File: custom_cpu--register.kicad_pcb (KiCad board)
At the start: 2 copper layers, 100 x 63 mm, 45 parts, among them P1 CONN_01X01, P10 CONN_01X01, P11 CONN_01X01, P12 CONN_01X01, P13 CONN_01X01, P14 CONN_01X01, P15 CONN_01X01, P16 CONN_01X01, P17 CONN_01X01, P18 CONN_01X01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

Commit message: Finish preliminary design
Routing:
- net VCC: track 0.00 -> 118.2 mm, vias 0 -> 3
- net Net-(P7-Pad1): track 0.00 -> 75.4 mm, vias 0 -> 3
- net Net-(P5-Pad1): track 0.00 -> 64.7 mm
- net Net-(P12-Pad1): track 0.00 -> 60.7 mm, vias 0 -> 1
- net Net-(D8-Pad2): track 0.00 -> 59.7 mm, vias 0 -> 1
- net Net-(P1-Pad1): track 0.00 -> 57.0 mm, vias 0 -> 2
- net Net-(D1-Pad2): track 0.00 -> 52.3 mm, vias 0 -> 2
- net Net-(P6-Pad1): track 0.00 -> 52.0 mm, vias 0 -> 2
- net Net-(D7-Pad2): track 0.00 -> 51.6 mm, vias 0 -> 2
- net Net-(P8-Pad1): track 0.00 -> 49.8 mm, vias 0 -> 2
- net Net-(P2-Pad1): track 0.00 -> 49.1 mm, vias 0 -> 2
- net Net-(P13-Pad1): track 0.00 -> 45.5 mm
- net Net-(D6-Pad2): track 0.00 -> 44.2 mm, vias 0 -> 2
- net Net-(P9-Pad1): track 0.00 -> 43.9 mm, vias 0 -> 2
- net Net-(D2-Pad2): track 0.00 -> 42.5 mm, vias 0 -> 2
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- added copper zone on B.Cu, net GND
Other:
- board text added: "CPU Register"
- board text added: "Fake resistors, use wire"
- board text added: "Register design - Ben Eater KiCAD layout - Leland Batey"

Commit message: Tweak trace layout, add PNG version of layout
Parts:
- moved P23 0.27 mm to (54.0, 55.3)
- moved P25 0.27 mm to (146.0, 55.3)
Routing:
- net Net-(D8-Pad2): track 59.7 -> 56.0 mm
- net VCC: track 118.2 -> 121.5 mm
- net Net-(D1-Pad2): track 52.3 -> 54.4 mm
- net Net-(D3-Pad2): track 35.2 -> 37.0 mm
- net Net-(D6-Pad2): track 44.2 -> 46.0 mm
- net Net-(D2-Pad2): track 42.5 -> 44.3 mm
- net Net-(D4-Pad2): track 30.7 -> 32.1 mm
- net Net-(D5-Pad2): track 40.0 -> 40.9 mm

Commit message: Make labels consistent with original design, add README
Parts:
- removed P1, P14, P15, P16, P17, P18, P19, P2, P20, P21, P3, P4, P5, P6, P7, P8: CONN_01X01, Connectors:PINTST
- added D_inpt_1: CONN_01X01, Connectors:PINTST, F.Cu at (54.0, 65.0)
- added D_inpt_2: CONN_01X01, Connectors:PINTST, F.Cu at (54.0, 69.0)
- added D_inpt_3: CONN_01X01, Connectors:PINTST, F.Cu at (54.0, 73.0)
- added D_inpt_4: CONN_01X01, Connectors:PINTST, F.Cu at (54.0, 77.0)
- added D_inpt_5: CONN_01X01, Connectors:PINTST, F.Cu at (54.0, 85.0)
- added D_inpt_6: CONN_01X01, Connectors:PINTST, F.Cu at (54.0, 89.0)
- added D_inpt_7: CONN_01X01, Connectors:PINTST, F.Cu at (54.0, 93.0)
- added D_inpt_8: CONN_01X01, Connectors:PINTST, F.Cu at (54.0, 97.0)
- added D_outpt_1: CONN_01X01, Connectors:PINTST, F.Cu at (147.0, 67.0)
- added D_outpt_2: CONN_01X01, Connectors:PINTST, F.Cu at (147.0, 71.0)
- added D_outpt_3: CONN_01X01, Connectors:PINTST, F.Cu at (147.0, 75.0)
- added D_outpt_4: CONN_01X01, Connectors:PINTST, F.Cu at (147.0, 79.0)
- added D_outpt_5: CONN_01X01, Connectors:PINTST, F.Cu at (147.0, 83.0)
- added D_outpt_6: CONN_01X01, Connectors:PINTST, F.Cu at (147.0, 87.0)
- added D_outpt_7: CONN_01X01, Connectors:PINTST, F.Cu at (147.0, 91.0)
- added D_outpt_8: CONN_01X01, Connectors:PINTST, F.Cu at (147.0, 95.0)
- moved R1 62.9 mm to (118.0, 66.0), turned to 180 degrees
- moved P11 52.8 mm to (80.0, 111.0)
- moved P9 52.3 mm to (90.0, 111.0)
- moved P10 52.2 mm to (85.0, 111.0)
- moved R9 47.8 mm to (73.0, 110.0), turned to 90 degrees
- moved R2 4.00 mm to (118.0, 70.0)
- moved R3 4.00 mm to (118.0, 74.0)
- moved R4 4.00 mm to (118.0, 78.0)
- moved R5 4.00 mm to (118.0, 82.0)
- moved R6 4.00 mm to (118.0, 86.0)
- moved R7 4.00 mm to (118.0, 90.0)
- moved R8 4.00 mm to (118.0, 94.0)
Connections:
- R1 pad 1: Net-(P12-Pad1) -> Net-(R1-Pad1)
- R1 pad 2: GND -> Net-(D1-Pad2)
- R2 pad 2: Net-(D1-Pad2) -> Net-(D2-Pad2)
- R3 pad 2: Net-(D2-Pad2) -> Net-(D3-Pad2)
- R4 pad 2: Net-(D3-Pad2) -> Net-(D4-Pad2)
- R5 pad 2: Net-(D4-Pad2) -> Net-(D5-Pad2)
- R6 pad 2: Net-(D5-Pad2) -> Net-(D6-Pad2)
- R7 pad 2: Net-(D6-Pad2) -> Net-(D7-Pad2)
- R8 pad 2: Net-(D7-Pad2) -> Net-(D8-Pad2)
- R9 pad 1: Net-(R9-Pad1) -> Net-(P12-Pad1)
- R9 pad 2: Net-(D8-Pad2) -> GND
- U1 pad 10: Net-(P5-Pad1) -> Net-(P9-Pad1)
- U1 pad 12: Net-(P9-Pad1) -> Net-(D_inpt_3-Pad1)
- U1 pad 13: Net-(P10-Pad1) -> Net-(D_inpt_2-Pad1)
- U1 pad 14: Net-(P11-Pad1) -> Net-(D_inpt_1-Pad1)
- U1 pad 15: Net-(P7-Pad1) -> Net-(P11-Pad1)
- U1 pad 7: Net-(P6-Pad1) -> Net-(P10-Pad1)
- U1 pad 9: Net-(P5-Pad1) -> Net-(P9-Pad1)
- U2 pad 10: Net-(P5-Pad1) -> Net-(P9-Pad1)
- U2 pad 15: Net-(P7-Pad1) -> Net-(P11-Pad1)
- U2 pad 7: Net-(P6-Pad1) -> Net-(P10-Pad1)
- U2 pad 9: Net-(P5-Pad1) -> Net-(P9-Pad1)
- U3 pad 2: Net-(R2-Pad1) -> Net-(R1-Pad1)
- U3 pad 3: Net-(R3-Pad1) -> Net-(R2-Pad1)
- U3 pad 4: Net-(R4-Pad1) -> Net-(R3-Pad1)
- U3 pad 5: Net-(R5-Pad1) -> Net-(R4-Pad1)
- U3 pad 6: Net-(R6-Pad1) -> Net-(R5-Pad1)
- U3 pad 7: Net-(R7-Pad1) -> Net-(R6-Pad1)
- U3 pad 8: Net-(R8-Pad1) -> Net-(R7-Pad1)
- U3 pad 9: Net-(R9-Pad1) -> Net-(R8-Pad1)
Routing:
- net Net-(P7-Pad1): track 75.4 -> 0.00 mm, vias 3 -> 0
- net Net-(P5-Pad1): track 64.7 -> 0.00 mm
- net Net-(P6-Pad1): track 52.0 -> 0.00 mm, vias 2 -> 0
- net Net-(P11-Pad1): track 30.9 -> 75.4 mm, vias 2 -> 3
- net Net-(D_inpt_3-Pad1): track 0.00 -> 43.9 mm, vias 0 -> 2
- net Net-(D_inpt_2-Pad1): track 0.00 -> 38.0 mm, vias 0 -> 2
- net Net-(D_inpt_1-Pad1): track 0.00 -> 30.9 mm, vias 0 -> 2
- net Net-(P9-Pad1): track 43.9 -> 64.7 mm, vias 2 -> 0
- net Net-(P10-Pad1): track 38.0 -> 52.0 mm
- net Net-(R1-Pad1): track 0.00 -> 10.7 mm
- net Net-(R9-Pad1): track 10.3 -> 0.00 mm
- net Net-(R8-Pad1): track 9.66 -> 10.3 mm
- net Net-(R6-Pad1): track 8.45 -> 9.05 mm
- net Net-(R2-Pad1): track 10.7 -> 10.1 mm
- net Net-(R4-Pad1): track 9.52 -> 8.92 mm
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
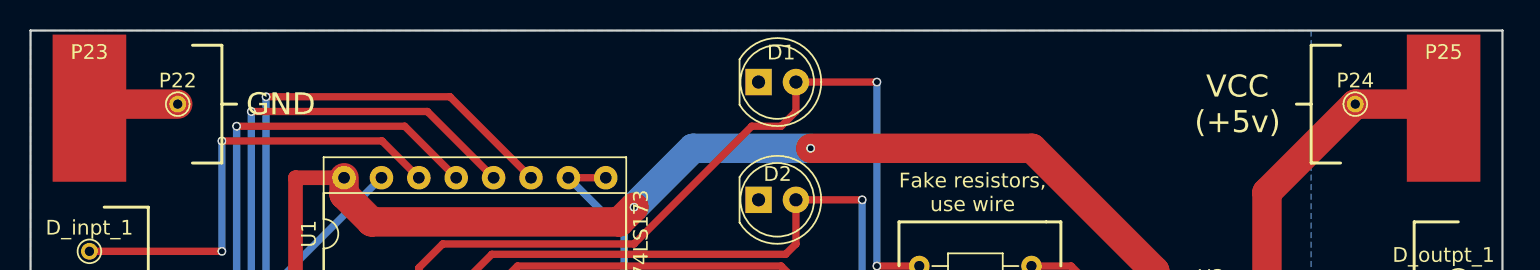
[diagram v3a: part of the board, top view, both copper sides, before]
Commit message: Added redundant power pads to back of board
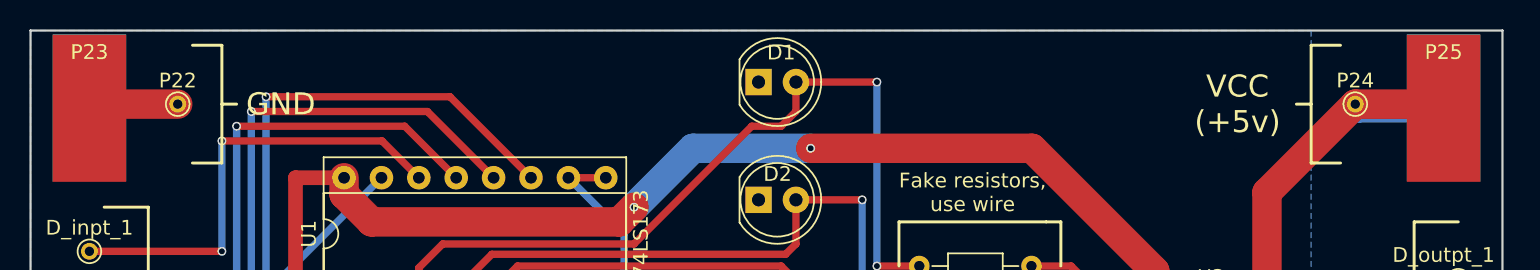
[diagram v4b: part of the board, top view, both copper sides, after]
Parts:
- added P1: CONN_01X01, Wire_Pads:SolderWirePad_single_SMD_5x10mm, B.Cu at (54.0, 55.2)
- added P2: CONN_01X01, Wire_Pads:SolderWirePad_single_SMD_5x10mm, B.Cu at (146.0, 55.2)
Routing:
- net VCC: track 121.5 -> 127.6 mm
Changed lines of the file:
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@@
 (kicad_pcb (version 4) (host pcbnew 4.0.5-e0-6337~49~ubuntu16.04.1)
   (general
-    (links 72)
+    (links 74)
     (no_connects 0)
-    (area 36.435716 49.799999 152.033334 157.700001)
+    (area 49.924999 49.924999 150.075001 113.075001)
     (thickness 1.6)
     (drawings 53)
-    (tracks 243)
+    (tracks 245)
     (zones 0)
-    (modules 45)
+    (modules 47)
     (nets 40)
   )
@@
   )
   (setup
-    (last_trace_width 0.5)
+    (last_trace_width 2)
     (user_trace_width 0.25)
     (user_trace_width 0.5)
@@
     )
   )
+  (module Wire_Pads:SolderWirePad_single_SMD_5x10mm (layer B.Cu)
+    (at 54 55.25)
+    (descr "Wire Pad, Square, SMD Pad,  5mm x 10mm,")
+    (tags "MesurementPoint Square SMDPad 5mmx10mm ")
+    (attr smd)
+    (fp_text reference P1 (at 0 3.81) (layer B.SilkS)
+      (effects (font (size 1 1) (thickness 0.15)) (justify mirror))
+    )
+    (fp_text value CONN_01X01 (at 0 -6.35) (layer B.Fab)
+      (effects (font (size 1 1) (thickness 0.15)) (justify mirror))
+    )
+    (fp_line (start 2.75 5.25) (end -2.75 5.25) (layer B.CrtYd) (width 0.05))
+    (fp_line (start 2.75 -5.25) (end 2.75 5.25) (layer B.CrtYd) (width 0.05))
+    (fp_line (start -2.75 -5.25) (end 2.75 -5.25) (layer B.CrtYd) (width 0.05))
+    (fp_line (start -2.75 5.25) (end -2.75 -5.25) (layer B.CrtYd) (width 0.05))
+    (pad 1 smd rect (at 0 0) (size 5 10) (layers B.Cu B.Paste B.Mask)
+      (net 6 GND))
+  )
+  (module Wire_Pads:SolderWirePad_single_SMD_5x10mm (layer B.Cu)
+    (at 146 55.25)
+    (descr "Wire Pad, Square, SMD Pad,  5mm x 10mm,")
+    (tags "MesurementPoint Square SMDPad 5mmx10mm ")
+    (attr smd)
+    (fp_text reference P2 (at 0 3.81) (layer B.SilkS)
+      (effects (font (size 1 1) (thickness 0.15)) (justify mirror))
+    )
+    (fp_text value CONN_01X01 (at 0 -6.35) (layer B.Fab)
+      (effects (font (size 1 1) (thickness 0.15)) (justify mirror))
+    )
+    (fp_line (start 2.75 5.25) (end -2.75 5.25) (layer B.CrtYd) (width 0.05))
+    (fp_line (start 2.75 -5.25) (end 2.75 5.25) (layer B.CrtYd) (width 0.05))
+    (fp_line (start -2.75 -5.25) (end 2.75 -5.25) (layer B.CrtYd) (width 0.05))
+    (fp_line (start -2.75 5.25) (end -2.75 -5.25) (layer B.CrtYd) (width 0.05))
+    (pad 1 smd rect (at 0 0) (size 5 10) (layers B.Cu B.Paste B.Mask)
+      (net 7 VCC))
+  )
   (gr_text "Fake resistors,\nuse wire" (at 114 61) (layer F.SilkS)
     (effects (font (size 1 1) (thickness 0.2)))
@@
   (segment (start 99.46 68.1) (end 99.46 69.5) (width 0.5) (layer F.Cu) (net 6))
   (segment (start 54 55) (end 60 55) (width 2) (layer F.Cu) (net 6))
+  (segment (start 146 55.25) (end 140.25 55.25) (width 2) (layer B.Cu) (net 7))
+  (segment (start 140.25 55.25) (end 140 55) (width 2) (layer B.Cu) (net 7))
   (segment (start 72 71) (end 72 77.76) (width 1) (layer B.Cu) (net 7))
   (segment (start 72 77.76) (end 71.38 78.38) (width 1) (layer B.Cu) (net 7))

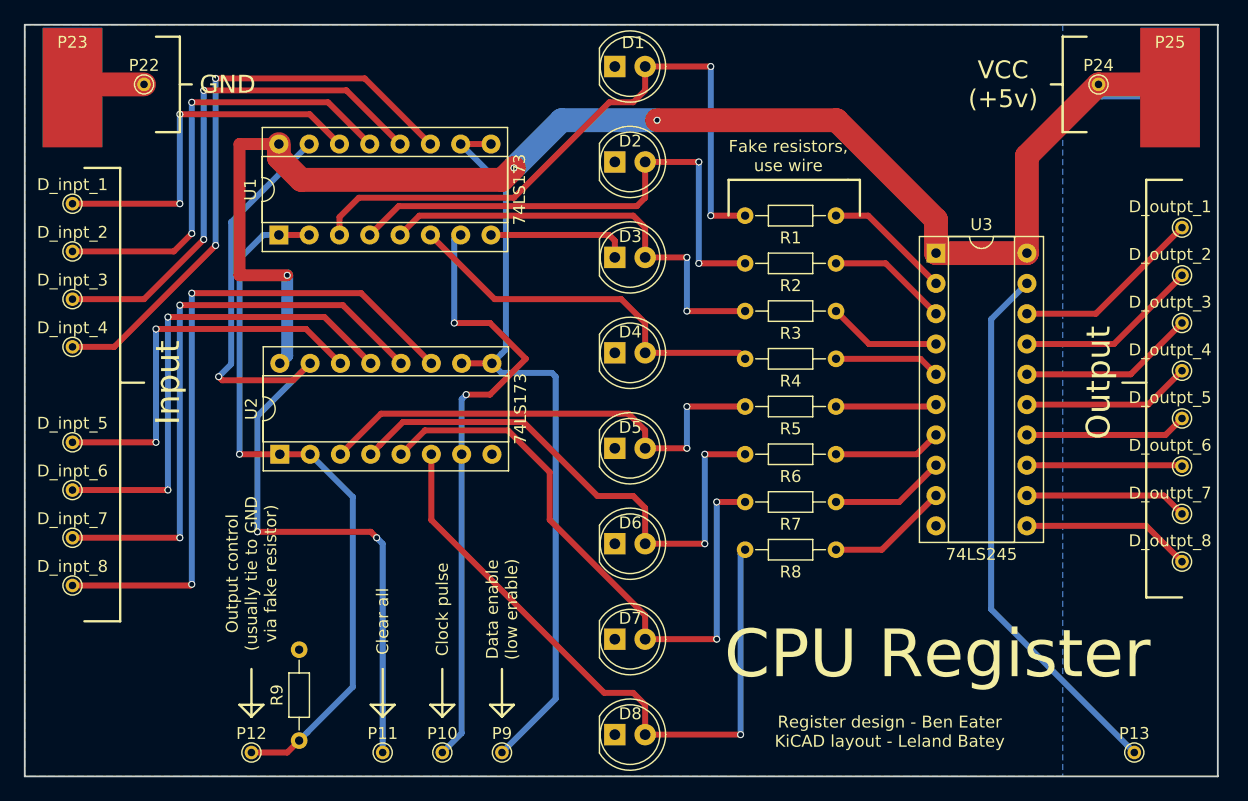
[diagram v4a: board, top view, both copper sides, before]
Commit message: Add output control label
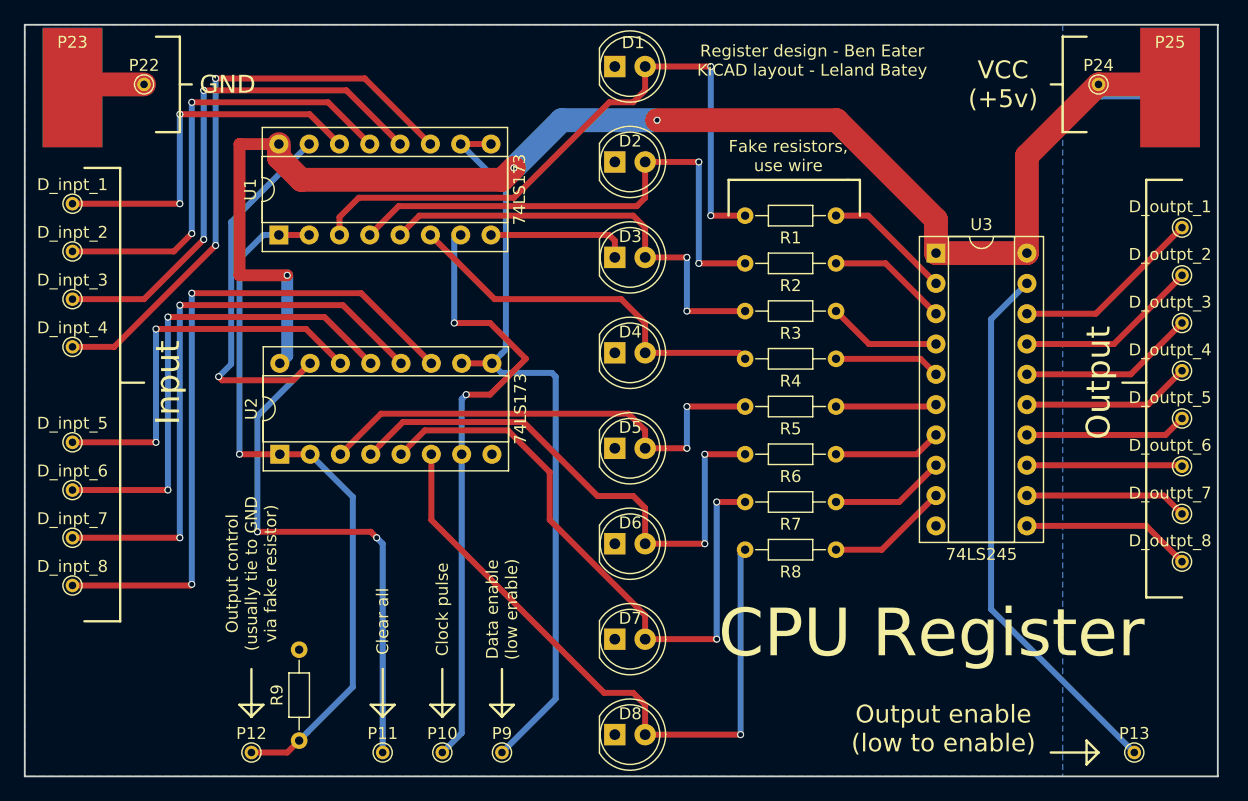
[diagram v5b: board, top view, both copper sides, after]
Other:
- board text added: "Output enable (low to enable)"
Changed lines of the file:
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@@
     (links 74)
     (no_connects 0)
-    (area 49.924999 49.924999 150.075001 113.075001)
+    (area 36.435716 47.925 152.033334 157.700001)
     (thickness 1.6)
-    (drawings 53)
+    (drawings 58)
     (tracks 245)
     (zones 0)
@@
   )
   (setup
-    (last_trace_width 2)
+    (last_trace_width 0.25)
     (user_trace_width 0.25)
     (user_trace_width 0.5)
@@
       (net 7 VCC))
   )
+  (gr_line (start 139 112) (end 140 111) (layer F.SilkS) (width 0.2))
+  (gr_line (start 136 111) (end 140 111) (layer F.SilkS) (width 0.2))
+  (gr_line (start 140 111) (end 139 110) (layer F.SilkS) (width 0.2))
+  (gr_line (start 139 110) (end 139 112) (layer F.SilkS) (width 0.2))
+  (gr_text "Output enable\n(low to enable)" (at 127 109) (layer F.SilkS)
+    (effects (font (size 1.5 1.5) (thickness 0.3)))
+  )
   (gr_text "Fake resistors,\nuse wire" (at 114 61) (layer F.SilkS)
     (effects (font (size 1 1) (thickness 0.2)))
@@
   (gr_line (start 109 63) (end 119 63) (layer F.SilkS) (width 0.2))
   (gr_line (start 109 66) (end 109 63) (layer F.SilkS) (width 0.2))
-  (gr_text "CPU Register" (at 126.5 102.75) (layer F.SilkS)
+  (gr_text "CPU Register" (at 126 101) (layer F.SilkS)
     (effects (font (size 4 4) (thickness 0.4)))
   )
-  (gr_text "Register design - Ben Eater\nKiCAD layout - Leland Batey" (at 122.5 109.25) (layer F.SilkS)
+  (gr_text "Register design - Ben Eater\nKiCAD layout - Leland Batey" (at 116 53) (layer F.SilkS)
     (effects (font (size 1 1) (thickness 0.2)))
   )
